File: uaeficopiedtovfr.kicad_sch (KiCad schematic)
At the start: 33 parts, among them J1 DTF13-12PB, J1 USB_B_Mini, J1 USB_C_Receptacle_USB2.0, J17 Conn_01x06, J4 DTF13-12PB, J5 Conn_01x05_Male, M1 Module-power_12and5V-0.2, M3 Module-knock-0.2, M3 Module-vr-discrete-0.4, M4 Module-vr-max9924-0.1, M5 Module-wbo-0.5, M6 Module:mega-mcu100/0.2, M7 Module-wbo-0.5, P1 Pad, P2 Pad, P3 Pad, P4 Pad, U4 JDY-33

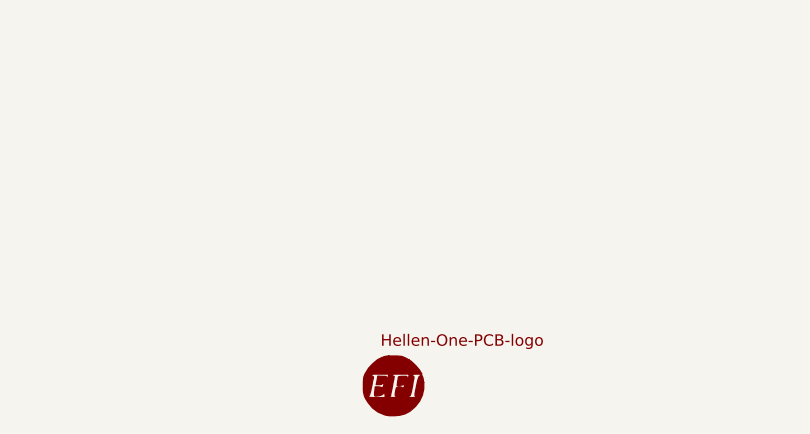
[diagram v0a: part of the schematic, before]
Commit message: added ref to graphics
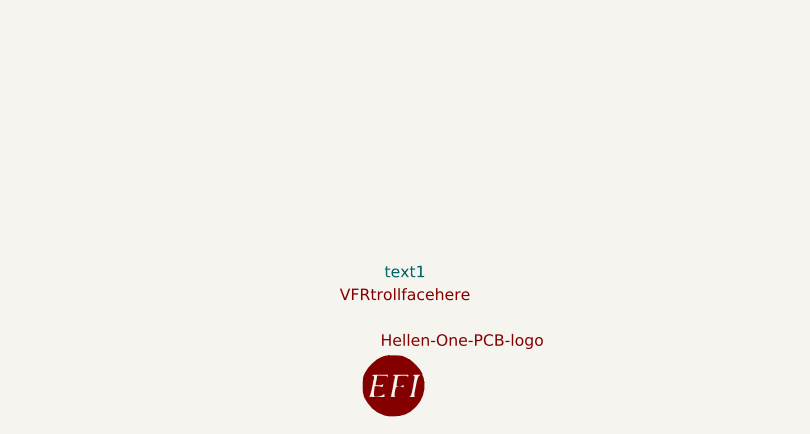
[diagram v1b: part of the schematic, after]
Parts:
- added text1: ~, Customparts:trollfaceVFR, symbol customparts:trollfacevfr
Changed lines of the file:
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@@
+    )
+  )
+  (symbol (lib_id "customparts:trollfacevfr") (at 275.59 388.62 0) (unit 1)
+    (in_bom yes) (on_board yes) (dnp no) (fields_autoplaced)
+    (property "Reference" "text1" (at 275.59 383.54 0)
+      (effects (font (size 1.27 1.27)))
+    )
+    (property "Value" "~" (at 275.59 388.62 0)
+      (effects (font (size 1.27 1.27)))
+    )
+    (property "Footprint" "Customparts:trollfaceVFR" (at 275.59 388.62 0)
+      (effects (font (size 1.27 1.27)) hide)
+    )
+    (property "Datasheet" "" (at 275.59 388.62 0)
+      (effects (font (size 1.27 1.27)) hide)
+    )
+    (instances
+      (project "uaeficopiedtovfr"
+        (path "/90b72e19-92bc-40db-bd4d-f17fb5de93ea"
+          (reference "text1") (unit 1)
+        )
+      )
     )
   )

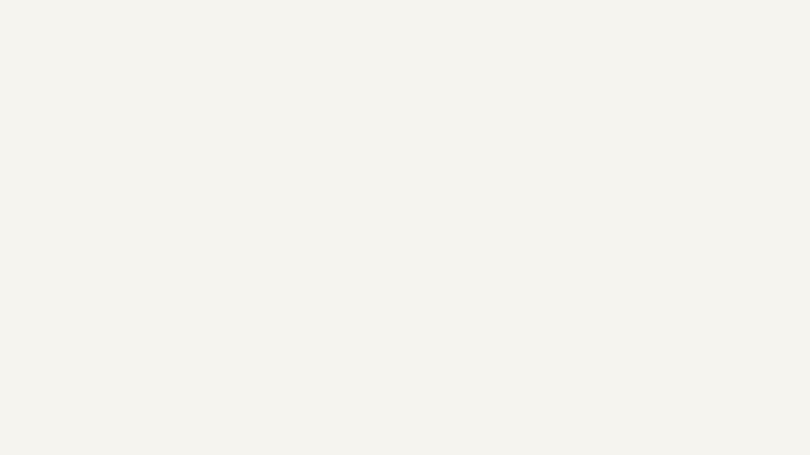
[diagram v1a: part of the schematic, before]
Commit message: Added mounting holes
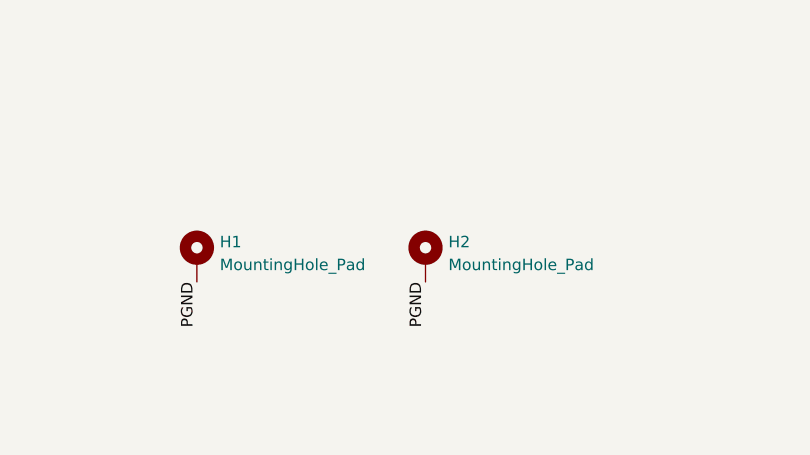
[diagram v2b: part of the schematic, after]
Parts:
- added H1, H2: MountingHole_Pad, MountingHole:MountingHole_3.2mm_M3_DIN965_Pad, symbol Mechanical:MountingHole_Pad
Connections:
- net GND: now also H1.1, H2.1
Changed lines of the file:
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@@
     (effects (font (size 1.27 1.27)) (justify left bottom))
+  )
+  (label "PGND" (at 156.21 382.27 270) (fields_autoplaced)
+    (effects (font (size 1.27 1.27)) (justify right bottom))
   )
   (label "IN_HALL2" (at 273.05 242.57 180) (fields_autoplaced)
@@
   )
   (label "PG_5VP" (at 349.25 130.81 180) (fields_autoplaced)
+    (effects (font (size 1.27 1.27)) (justify right bottom))
+  )
+  (label "PGND" (at 130.81 382.27 270) (fields_autoplaced)
     (effects (font (size 1.27 1.27)) (justify right bottom))
   )
@@
         (path "/ac264c30-3e9a-4be2-b97a-9949b68bd497"
           (reference "#PWR014") (unit 1)
+        )
+      )
+    )
+  )
+  (symbol (lib_id "Mechanical:MountingHole_Pad") (at 156.21 379.73 0) (unit 1)
+    (in_bom yes) (on_board yes) (dnp no) (fields_autoplaced)
+    (property "Reference" "H2" (at 158.75 377.825 0)
+      (effects (font (size 1.27 1.27)) (justify left))
+    )
+    (property "Value" "MountingHole_Pad" (at 158.75 380.365 0)
+      (effects (font (size 1.27 1.27)) (justify left))
+    )
+    (property "Footprint" "MountingHole:MountingHole_3.2mm_M3_DIN965_Pad" (at 156.21 379.73 0)
+      (effects (font (size 1.27 1.27)) hide)
+    )
+    (property "Datasheet" "~" (at 156.21 379.73 0)
+      (effects (font (size 1.27 1.27)) hide)
+    )
+    (pin "1")
+    (instances
+      (project "uaeficopiedtovfr"
+        (path "/90b72e19-92bc-40db-bd4d-f17fb5de93ea"
+          (reference "H2") (unit 1)
         )
       )
@@
         )
       )
+    )
+  )
+  (symbol (lib_id "Mechanical:MountingHole_Pad") (at 130.81 379.73 0) (unit 1)
+    (in_bom yes) (on_board yes) (dnp no) (fields_autoplaced)
+    (property "Reference" "H1" (at 133.35 377.825 0)
+      (effects (font (size 1.27 1.27)) (justify left))
+    )
+    (property "Value" "MountingHole_Pad" (at 133.35 380.365 0)
+      (effects (font (size 1.27 1.27)) (justify left))
+    )
+    (property "Footprint" "MountingHole:MountingHole_3.2mm_M3_DIN965_Pad" (at 130.81 379.73 0)
+      (effects (font (size 1.27 1.27)) hide)
+    )
+    (property "Datasheet" "~" (at 130.81 379.73 0)
+      (effects (font (size 1.27 1.27)) hide)
+    )
+    (pin "1")
+    (instances
+      (project "uaeficopiedtovfr"
+        (path "/90b72e19-92bc-40db-bd4d-f17fb5de93ea"
+          (reference "H1") (unit 1)
+        )
+      )

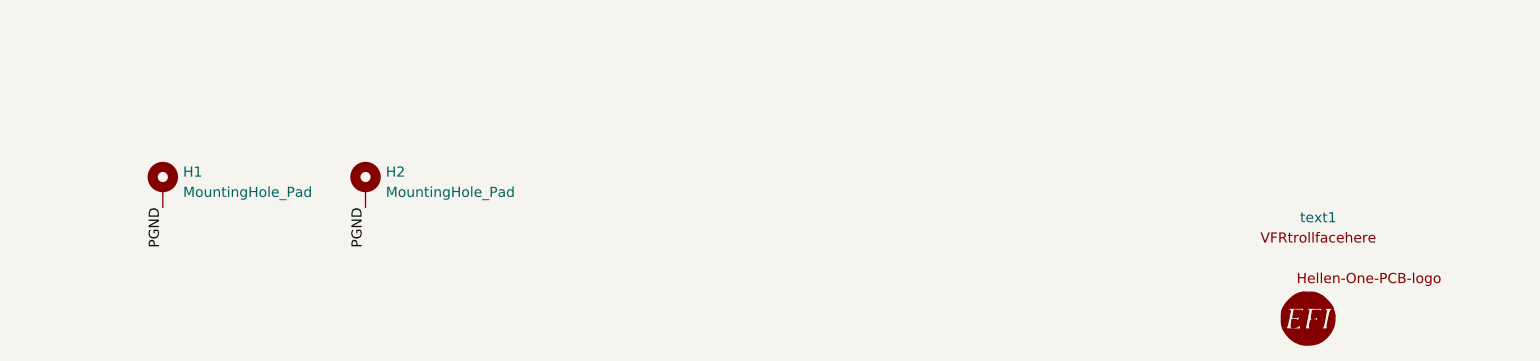
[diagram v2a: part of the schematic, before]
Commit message: generate 4 layer board
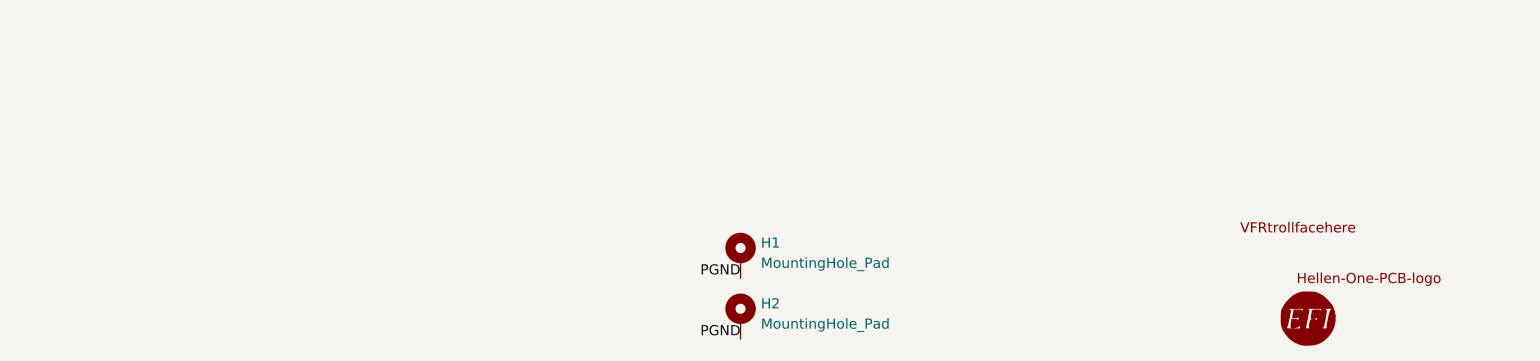
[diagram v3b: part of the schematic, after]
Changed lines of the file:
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@@
     (effects (font (size 1.27 1.27)) (justify right bottom))
   )
+  (label "PGND" (at 203.2 398.78 180) (fields_autoplaced)
+    (effects (font (size 1.27 1.27)) (justify right bottom))
+  )
   (label "PGND" (at 33.02 190.5 180) (fields_autoplaced)
     (effects (font (size 1.27 1.27)) (justify right bottom))
@@
     (effects (font (size 1.27 1.27)) (justify left bottom))
   )
-  (label "PGND" (at 156.21 382.27 270) (fields_autoplaced)
-    (effects (font (size 1.27 1.27)) (justify right bottom))
-  )
   (label "IN_HALL2" (at 273.05 242.57 180) (fields_autoplaced)
     (effects (font (size 1.27 1.27)) (justify right bottom))
@@
     (effects (font (size 1.27 1.27)) (justify left bottom))
   )
-  (label "PG_5VP" (at 349.25 130.81 180) (fields_autoplaced)
+  (label "PGND" (at 203.2 391.16 180) (fields_autoplaced)
     (effects (font (size 1.27 1.27)) (justify right bottom))
   )
-  (label "PGND" (at 130.81 382.27 270) (fields_autoplaced)
+  (label "PG_5VP" (at 349.25 130.81 180) (fields_autoplaced)
     (effects (font (size 1.27 1.27)) (justify right bottom))
   )
@@
     )
   )
-  (symbol (lib_id "Mechanical:MountingHole_Pad") (at 156.21 379.73 0) (unit 1)
-    (in_bom yes) (on_board yes) (dnp no) (fields_autoplaced)
-    (property "Reference" "H2" (at 158.75 377.825 0)
-      (effects (font (size 1.27 1.27)) (justify left))
-    )
-    (property "Value" "MountingHole_Pad" (at 158.75 380.365 0)
-      (effects (font (size 1.27 1.27)) (justify left))
-    )
-    (property "Footprint" "MountingHole:MountingHole_3.2mm_M3_DIN965_Pad" (at 156.21 379.73 0)
-      (effects (font (size 1.27 1.27)) hide)
-    )
-    (property "Datasheet" "~" (at 156.21 379.73 0)
-      (effects (font (size 1.27 1.27)) hide)
-    )
-    (pin "1")
-    (instances
-      (project "uaeficopiedtovfr"
-        (path "/90b72e19-92bc-40db-bd4d-f17fb5de93ea"
-          (reference "H2") (unit 1)
-        )
-      )
-    )
-  )
   (symbol (lib_id "power:+5VA") (at 341.63 252.73 270) (mirror x) (unit 1)
     (in_bom yes) (on_board yes) (dnp no)
@@
     )
   )
+  (symbol (lib_id "Mechanical:MountingHole_Pad") (at 203.2 388.62 0) (unit 1)
+    (in_bom yes) (on_board yes) (dnp no) (fields_autoplaced)
+    (property "Reference" "H1" (at 205.74 386.715 0)
+      (effects (font (size 1.27 1.27)) (justify left))
+    )
+    (property "Value" "MountingHole_Pad" (at 205.74 389.255 0)
+      (effects (font (size 1.27 1.27)) (justify left))
+    )
+    (property "Footprint" "MountingHole:MountingHole_3.2mm_M3_DIN965_Pad" (at 203.2 388.62 0)
+      (effects (font (size 1.27 1.27)) hide)
+    )
+    (property "Datasheet" "~" (at 203.2 388.62 0)
+      (effects (font (size 1.27 1.27)) hide)
+    )
+    (pin "1")
+    (instances
+      (project "uaeficopiedtovfr"
+        (path "/90b72e19-92bc-40db-bd4d-f17fb5de93ea"
+          (reference "H1") (unit 1)
+        )
+      )
+    )
+  )
   (symbol (lib_id "power:+5V") (at 273.05 273.05 90) (mirror x) (unit 1)
     (in_bom yes) (on_board yes) (dnp no)
@@
     )
   )
-  (symbol (lib_id "Mechanical:MountingHole_Pad") (at 130.81 379.73 0) (unit 1)
-    (in_bom yes) (on_board yes) (dnp no) (fields_autoplaced)
-    (property "Reference" "H1" (at 133.35 377.825 0)
-      (effects (font (size 1.27 1.27)) (justify left))
-    )
-    (property "Value" "MountingHole_Pad" (at 133.35 380.365 0)
-      (effects (font (size 1.27 1.27)) (justify left))
-    )
-    (property "Footprint" "MountingHole:MountingHole_3.2mm_M3_DIN965_Pad" (at 130.81 379.73 0)
-      (effects (font (size 1.27 1.27)) hide)
-    )
-    (property "Datasheet" "~" (at 130.81 379.73 0)
-      (effects (font (size 1.27 1.27)) hide)
-    )
-    (pin "1")
-    (instances
-      (project "uaeficopiedtovfr"
-        (path "/90b72e19-92bc-40db-bd4d-f17fb5de93ea"
-          (reference "H1") (unit 1)
-        )
-      )
-    )
-  )
   (symbol (lib_id "power:+12V") (at 168.91 148.59 0) (unit 1)
     (in_bom yes) (on_board yes) (dnp no)
@@
     )
   )
+  (symbol (lib_id "customparts:trollfacevfr") (at 273.05 387.35 0) (unit 1)
+    (in_bom yes) (on_board yes) (dnp no) (fields_autoplaced)
+    (property "Reference" "text1" (at 273.05 382.27 0)
+      (effects (font (size 1.27 1.27)) hide)
+    )
+    (property "Value" "~" (at 273.05 387.35 0)
+      (effects (font (size 1.27 1.27)))
+    )
+    (property "Footprint" "Customparts:trollfaceVFR" (at 273.05 387.35 0)
+      (effects (font (size 1.27 1.27)) hide)
+    )
+    (property "Datasheet" "" (at 273.05 387.35 0)
+      (effects (font (size 1.27 1.27)) hide)
+    )
+    (instances
+      (project "uaeficopiedtovfr"
+        (path "/90b72e19-92bc-40db-bd4d-f17fb5de93ea"
+          (reference "text1") (unit 1)
+        )
+      )
+    )
+  )
   (symbol (lib_id "power:+5VA") (at 341.63 255.27 270) (mirror x) (unit 1)
     (in_bom yes) (on_board yes) (dnp no)
@@
     )
   )
-  (symbol (lib_id "customparts:trollfacevfr") (at 275.59 388.62 0) (unit 1)
-    (in_bom yes) (on_board yes) (dnp no) (fields_autoplaced)
-    (property "Reference" "text1" (at 275.59 383.54 0)
-      (effects (font (size 1.27 1.27)))
-    )
-    (property "Value" "~" (at 275.59 388.62 0)
-      (effects (font (size 1.27 1.27)))
-    )
-    (property "Footprint" "Customparts:trollfaceVFR" (at 275.59 388.62 0)
-      (effects (font (size 1.27 1.27)) hide)
-    )
-    (property "Datasheet" "" (at 275.59 388.62 0)
-      (effects (font (size 1.27 1.27)) hide)
-    )
-    (instances
-      (project "uaeficopiedtovfr"
-        (path "/90b72e19-92bc-40db-bd4d-f17fb5de93ea"
-          (reference "text1") (unit 1)
-        )
-      )
-    )
-  )
   (symbol (lib_id "power:GND") (at 190.5 303.53 0) (unit 1)
     (in_bom yes) (on_board yes) (dnp no)
@@
         )
       )
+    )
+  )
+  (symbol (lib_id "Mechanical:MountingHole_Pad") (at 203.2 396.24 0) (unit 1)
+    (in_bom yes) (on_board yes) (dnp no) (fields_autoplaced)
+    (property "Reference" "H2" (at 205.74 394.335 0)
+      (effects (font (size 1.27 1.27)) (justify left))
+    )
+    (property "Value" "MountingHole_Pad" (at 205.74 396.875 0)
+      (effects (font (size 1.27 1.27)) (justify left))
+    )
+    (property "Footprint" "MountingHole:MountingHole_3.2mm_M3_DIN965_Pad" (at 203.2 396.24 0)
+      (effects (font (size 1.27 1.27)) hide)
+    )
+    (property "Datasheet" "~" (at 203.2 396.24 0)
+      (effects (font (size 1.27 1.27)) hide)
+    )
+    (pin "1")
+    (instances
+      (project "uaeficopiedtovfr"
+        (path "/90b72e19-92bc-40db-bd4d-f17fb5de93ea"
+          (reference "H2") (unit 1)
+        )
+      )
